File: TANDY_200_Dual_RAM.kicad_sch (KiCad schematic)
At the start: 5 parts, among them J1 Conn_01x01_Male, J2 TANDY_26-3688, U1 628128_SOP32, U2 74LVC1G08

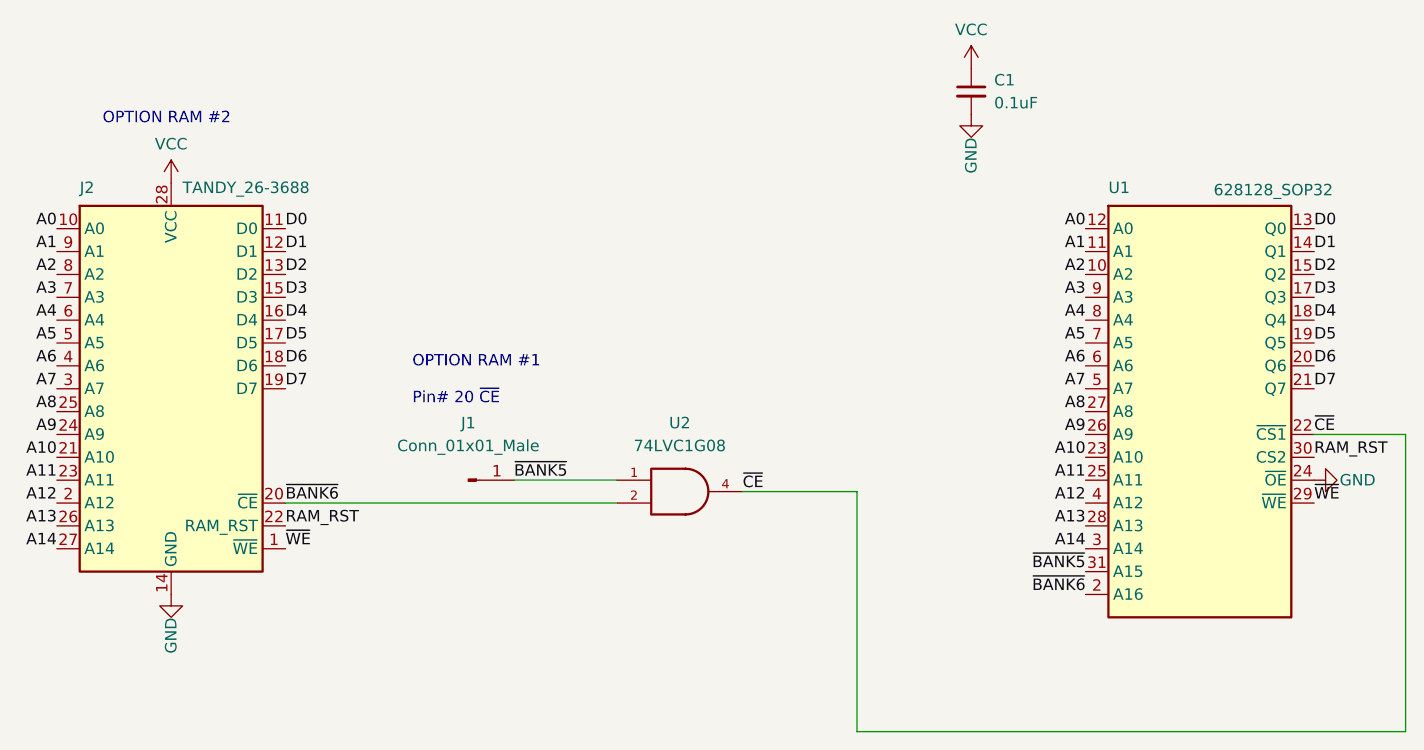
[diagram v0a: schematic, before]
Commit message: ground paths, footprints, sch symbols
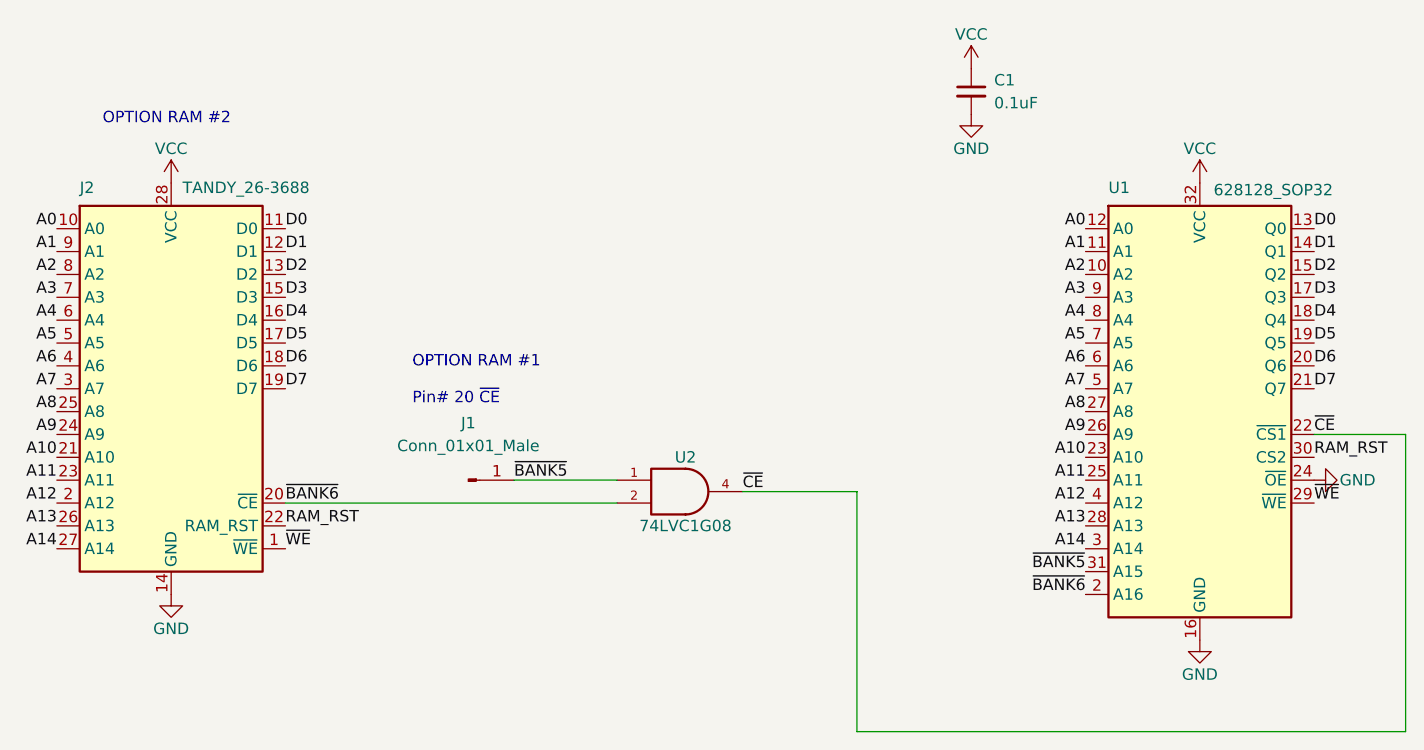
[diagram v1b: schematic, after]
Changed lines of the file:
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@@
       (effects (font (size 1.27 1.27)) hide)
     )
-    (property "Value" "VCC" (id 1) (at 76.2 74.422 0))
+    (property "Value" "VCC" (id 1) (at 76.2 74.93 0))
     (property "Footprint" "" (id 2) (at 76.2 78.74 0)
       (effects (font (size 1.27 1.27)) hide)
@@
       (effects (font (size 1.27 1.27)) hide)
     )
-    (property "Value" "GND" (id 1) (at 76.2 129.032 90))
+    (property "Value" "GND" (id 1) (at 76.2 128.27 0))
     (property "Footprint" "" (id 2) (at 76.2 124.46 0)
       (effects (font (size 1.27 1.27)) hide)
@@
     (pin "9")
   )
+  (symbol (lib_id "power:VCC") (at 190.5 78.74 0) (unit 1)
+    (in_bom yes) (on_board yes)
+    (property "Reference" "#PWR0103" (id 0) (at 190.5 82.55 0)
+      (effects (font (size 1.27 1.27)) hide)
+    )
+    (property "Value" "VCC" (id 1) (at 190.5 74.93 0))
+    (property "Footprint" "" (id 2) (at 190.5 78.74 0)
+      (effects (font (size 1.27 1.27)) hide)
+    )
+    (property "Datasheet" "" (id 3) (at 190.5 78.74 0)
+      (effects (font (size 1.27 1.27)) hide)
+    )
+    (pin "1")
+  )
   (symbol (lib_id "000_LOCAL:Conn_01x01_Male") (at 109.22 111.76 0) (unit 1)
     (in_bom yes) (on_board yes)
@@
     (pin "1")
   )
+  (symbol (lib_id "power:GND") (at 190.5 129.54 0) (unit 1)
+    (in_bom yes) (on_board yes)
+    (property "Reference" "#PWR0101" (id 0) (at 190.5 135.89 0)
+      (effects (font (size 1.27 1.27)) hide)
+    )
+    (property "Value" "GND" (id 1) (at 190.5 133.35 0))
+    (property "Footprint" "" (id 2) (at 190.5 129.54 0)
+      (effects (font (size 1.27 1.27)) hide)
+    )
+    (property "Datasheet" "" (id 3) (at 190.5 129.54 0)
+      (effects (font (size 1.27 1.27)) hide)
+    )
+    (pin "1")
+  )
   (symbol (lib_id "power:VCC") (at 165.1 66.04 0) (unit 1)
     (in_bom yes) (on_board yes)
@@
       (effects (font (size 1.27 1.27)) hide)
     )
-    (property "Value" "VCC" (id 1) (at 165.1 61.722 0))
+    (property "Value" "VCC" (id 1) (at 165.1 62.23 0))
     (property "Footprint" "" (id 2) (at 165.1 66.04 0)
       (effects (font (size 1.27 1.27)) hide)
@@
       (effects (font (size 1.27 1.27)) hide)
     )
-    (property "Value" "GND" (id 1) (at 165.1 75.692 90))
+    (property "Value" "GND" (id 1) (at 165.1 74.93 0))
     (property "Footprint" "" (id 2) (at 165.1 71.12 0)
       (effects (font (size 1.27 1.27)) hide)
@@
   )
   (symbol (lib_id "000_LOCAL:74LVC1G08") (at 133.35 113.03 0) (unit 1)
-    (in_bom yes) (on_board yes) (fields_autoplaced)
-    (property "Reference" "U2" (id 0) (at 132.715 105.41 0))
-    (property "Value" "74LVC1G08" (id 1) (at 132.715 107.95 0))
+    (in_bom yes) (on_board yes)
+    (property "Reference" "U2" (id 0) (at 133.35 109.22 0))
+    (property "Value" "74LVC1G08" (id 1) (at 133.35 116.84 0))
     (property "Footprint" "000_LOCAL:SOT-23-5" (id 2) (at 133.35 113.03 0)
       (effects (font (size 1.27 1.27)) hide)
@@
   )
   (symbol_instances
+    (path "/1fd2fa23-95e5-4589-9ecc-f933b4ca4e94"
+      (reference "#PWR0101") (unit 1) (value "GND") (footprint "")
+    )
     (path "/009aec29-5876-4a82-9c35-f7f614fcec3b"
       (reference "#PWR0102") (unit 1) (value "GND") (footprint "")
     )
+    (path "/108b3286-ae83-4aad-b412-4257c87e2146"
+      (reference "#PWR0103") (unit 1) (value "VCC") (footprint "")
+    )
     (path "/00000000-0000-0000-0000-000060782b2b"
